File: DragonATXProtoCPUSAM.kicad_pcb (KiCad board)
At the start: 2 copper layers, 151.2 x 56.7 mm, 17 parts, among them IC1 MC6809E, IC2 MC6883, IC3 74LS138, IC4 74LS02

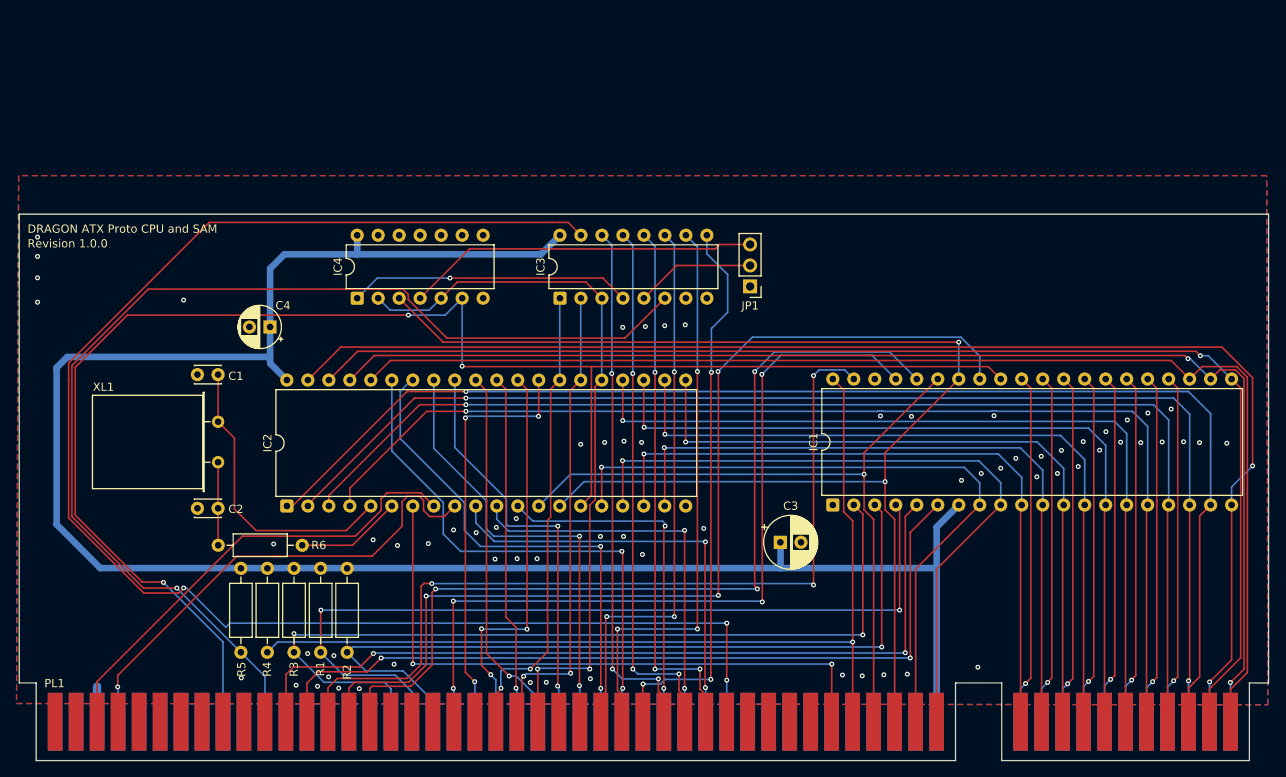
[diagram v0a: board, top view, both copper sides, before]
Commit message: add 256K banker
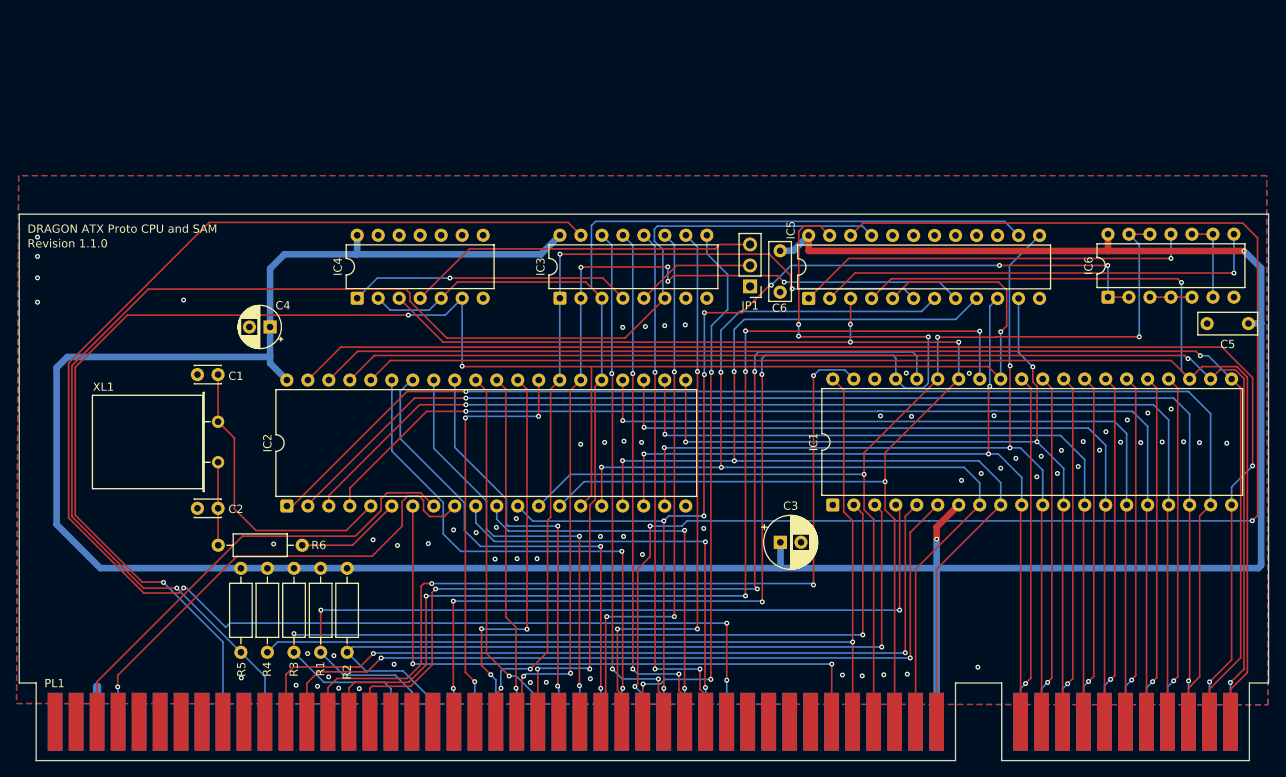
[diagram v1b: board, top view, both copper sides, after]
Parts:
- added C5: 100n, Capacitor_THT:C_Rect_L7.0mm_W2.5mm_P5.00mm, F.Cu at (233.2, 69.7)
- added C6: 100n, Capacitor_THT:C_Rect_L7.0mm_W2.5mm_P5.00mm, F.Cu at (176.6, 60.9)
- added IC5: GAL, Package_DIP:DIP-24_W7.62mm, F.Cu at (180.0, 66.7)
- added IC6: 74LS132, Package_DIP:DIP-14_W7.62mm, F.Cu at (216.3, 66.5)
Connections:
- PL1 pad b29: unconnected-(PL1A-Pin_b29-Padb29) -> /Z8
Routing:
- net /Z8: track 0.00 -> 183.1 mm, vias 0 -> 3
- net +5V: track 238.3 -> 379.0 mm, vias 0 -> 2
- net /RAS: track 43.1 -> 130.4 mm, vias 2 -> 8
- net /S2: track 88.6 -> 150.5 mm
- net /COLSEL: track 0.00 -> 54.9 mm, vias 0 -> 1
- net /S1: track 58.0 -> 110.3 mm, vias 2 -> 6
- net /S0: track 56.8 -> 108.0 mm, vias 2 -> 4
- net /A15: track 152.0 -> 202.8 mm, vias 0 -> 1
- net /~{Q}: track 0.00 -> 48.8 mm, vias 0 -> 1
- net /A1: track 84.9 -> 131.7 mm, vias 1 -> 3
- net /RST: track 98.4 -> 144.1 mm, vias 4 -> 7
- net /Q: track 87.0 -> 132.0 mm, vias 1 -> 3
- net /A0: track 83.8 -> 127.8 mm, vias 1 -> 3
- net /EXTMEN: track 135.9 -> 171.9 mm
- net /A3: track 84.9 -> 112.2 mm, vias 1 -> 3
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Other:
- board text added: "Revision 1.1.0"
- board text removed: "Revision 1.0.0"

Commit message: Include pull-up/down on data lines to allow quick forcing on selected inputs (for NOP)
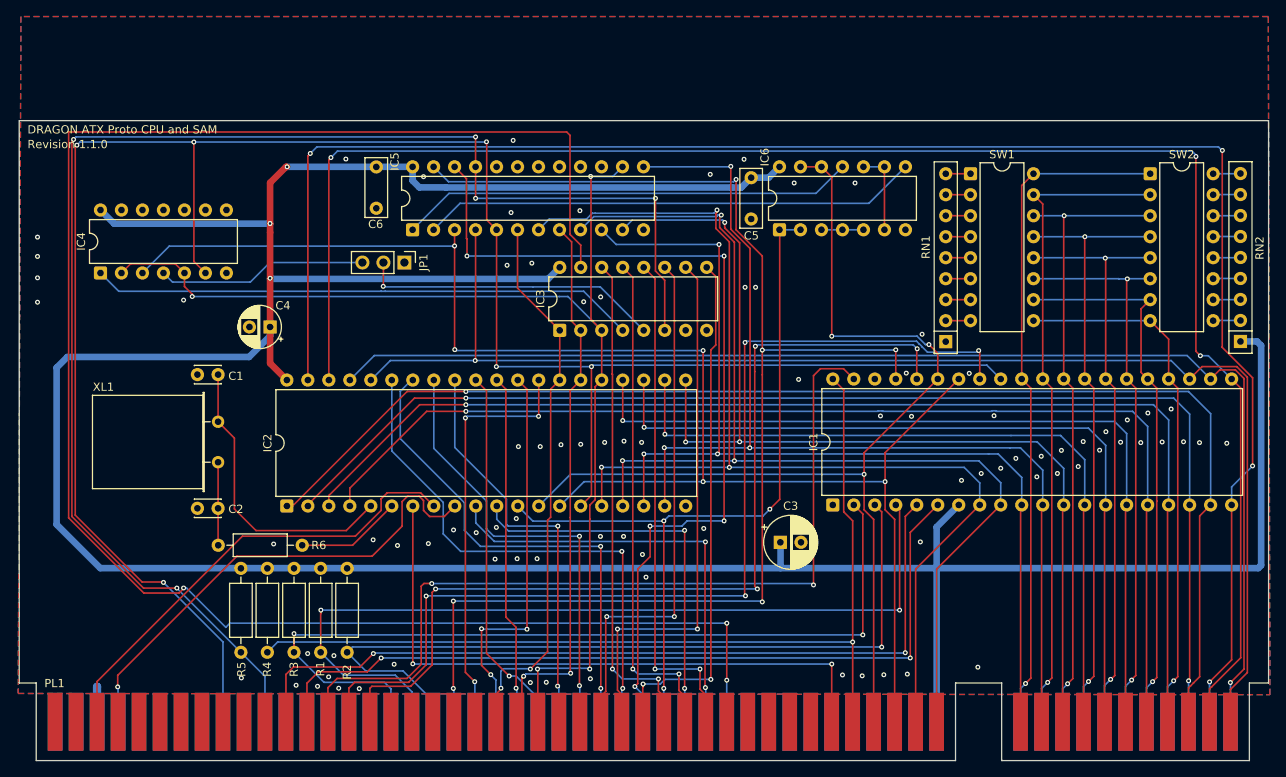
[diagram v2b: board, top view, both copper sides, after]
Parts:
- added RN1: 4K7, Resistor_THT:R_Array_SIP9, F.Cu at (196.6, 71.9)
- added RN2: 4K7, Resistor_THT:R_Array_SIP9, F.Cu at (232.3, 71.9)
- added SW1: DataValueLow, Package_DIP:DIP-16_W7.62mm, F.Cu at (199.6, 51.6)
- added SW2: DataValueHigh, Package_DIP:DIP-16_W7.62mm, F.Cu at (221.4, 51.6)
- moved C5 62.7 mm to (173.1, 52.1), turned to -90 degrees
- moved C6 49.9 mm to (127.7, 50.8)
- moved IC5 48.6 mm to (132.1, 58.4)
- moved JP1 41.9 mm to (131.1, 62.4), turned to -90 degrees
- moved IC6 40.6 mm to (176.5, 58.4)
- moved IC4 31.2 mm to (94.3, 63.6)
- moved IC3 3.89 mm to (149.9, 70.6)
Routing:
- net /Z8: track 183.1 -> 108.6 mm, vias 3 -> 5
- net /A12: track 161.7 -> 211.7 mm, vias 2 -> 4
- net /A13: track 156.0 -> 205.6 mm, vias 1 -> 3
- net /S1: track 110.3 -> 67.3 mm, vias 6 -> 2
- net /S0: track 108.0 -> 67.2 mm, vias 4 -> 2
- net /D0: track 42.8 -> 82.4 mm
- net /RAS: track 130.4 -> 93.4 mm, vias 8 -> 3
- net /D1: track 42.8 -> 79.7 mm
- net /D.OUT: track 186.6 -> 222.3 mm
- net /A15: track 202.8 -> 167.9 mm
- net /D2: track 42.9 -> 76.8 mm, vias 1 -> 2
- net /R/W: track 220.0 -> 252.2 mm, vias 4 -> 6
- net Net-(IC3-E1): track 34.2 -> 66.1 mm, vias 1 -> 0
- net /D3: track 42.8 -> 74.2 mm, vias 1 -> 2
- net /D4: track 42.8 -> 71.7 mm, vias 1 -> 2
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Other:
- board size 151.2 x 56.7 mm -> 151.2 x 68 mm
